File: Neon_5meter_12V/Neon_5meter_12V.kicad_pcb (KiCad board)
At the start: 2 copper layers, 77.5 x 51.5 mm, 47 parts, among them J2 Barrel_Jack_MountingPin, J4 Barrel_Jack_MountingPin, J5 Barrel_Jack_MountingPin, J6 Conn_01x03_Pin, Q1 IRLML2502TRPBF, Q2 IRLML2502TRPBF, Q3 BSS138, Q4 BSS138, Q5 BSS138, SW1 SW_Push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

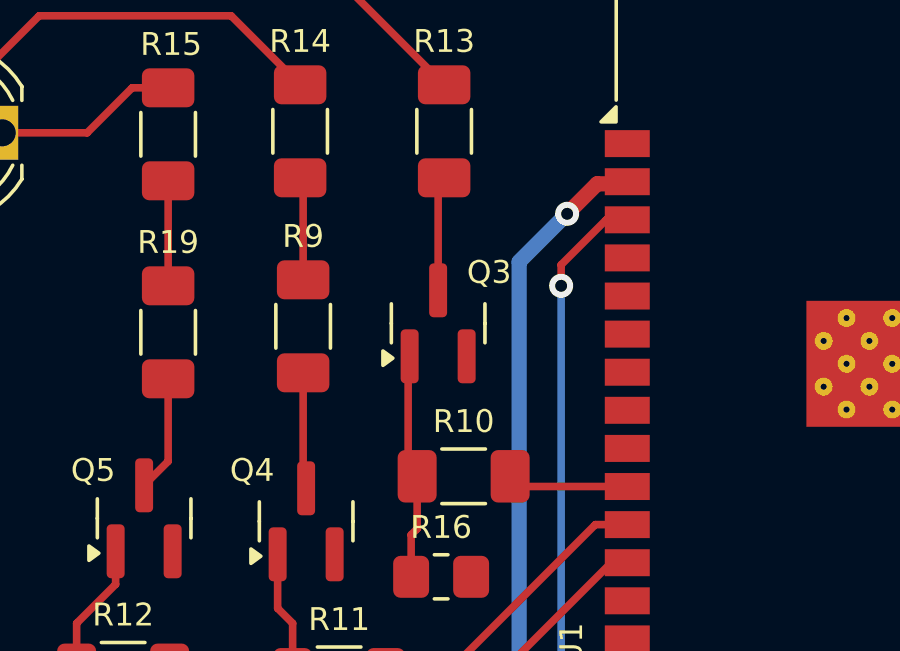
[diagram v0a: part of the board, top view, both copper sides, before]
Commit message: chnaged some of sot23 to be custom footprint to see which is better in hand soldering
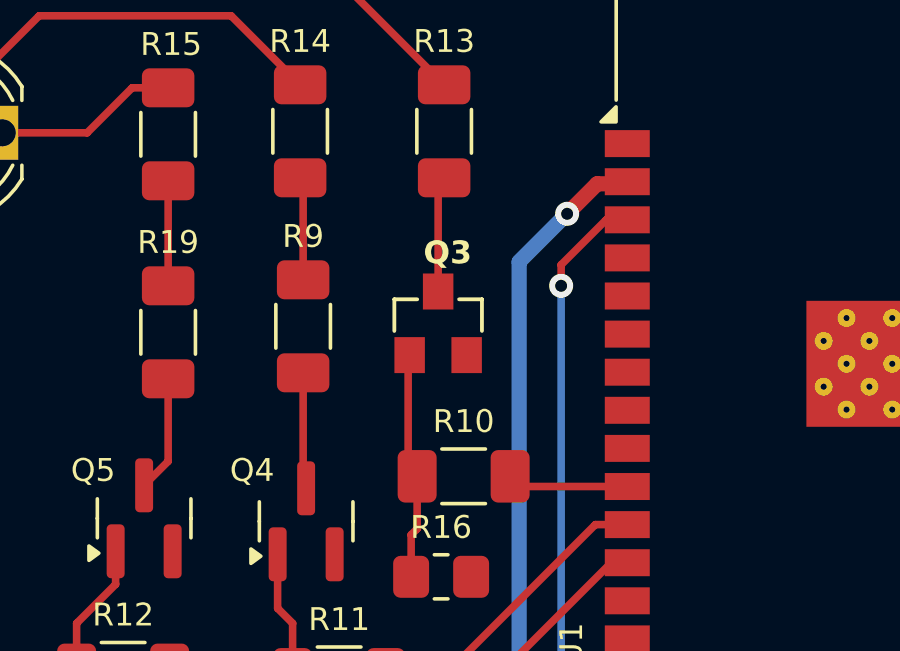
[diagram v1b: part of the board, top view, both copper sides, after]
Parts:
- Q3: footprint Package_TO_SOT_SMD:SOT-23 -> custom_SOT23:custom_SOT23
- turned Q3 to 0 degrees
